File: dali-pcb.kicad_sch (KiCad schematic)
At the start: 6 parts

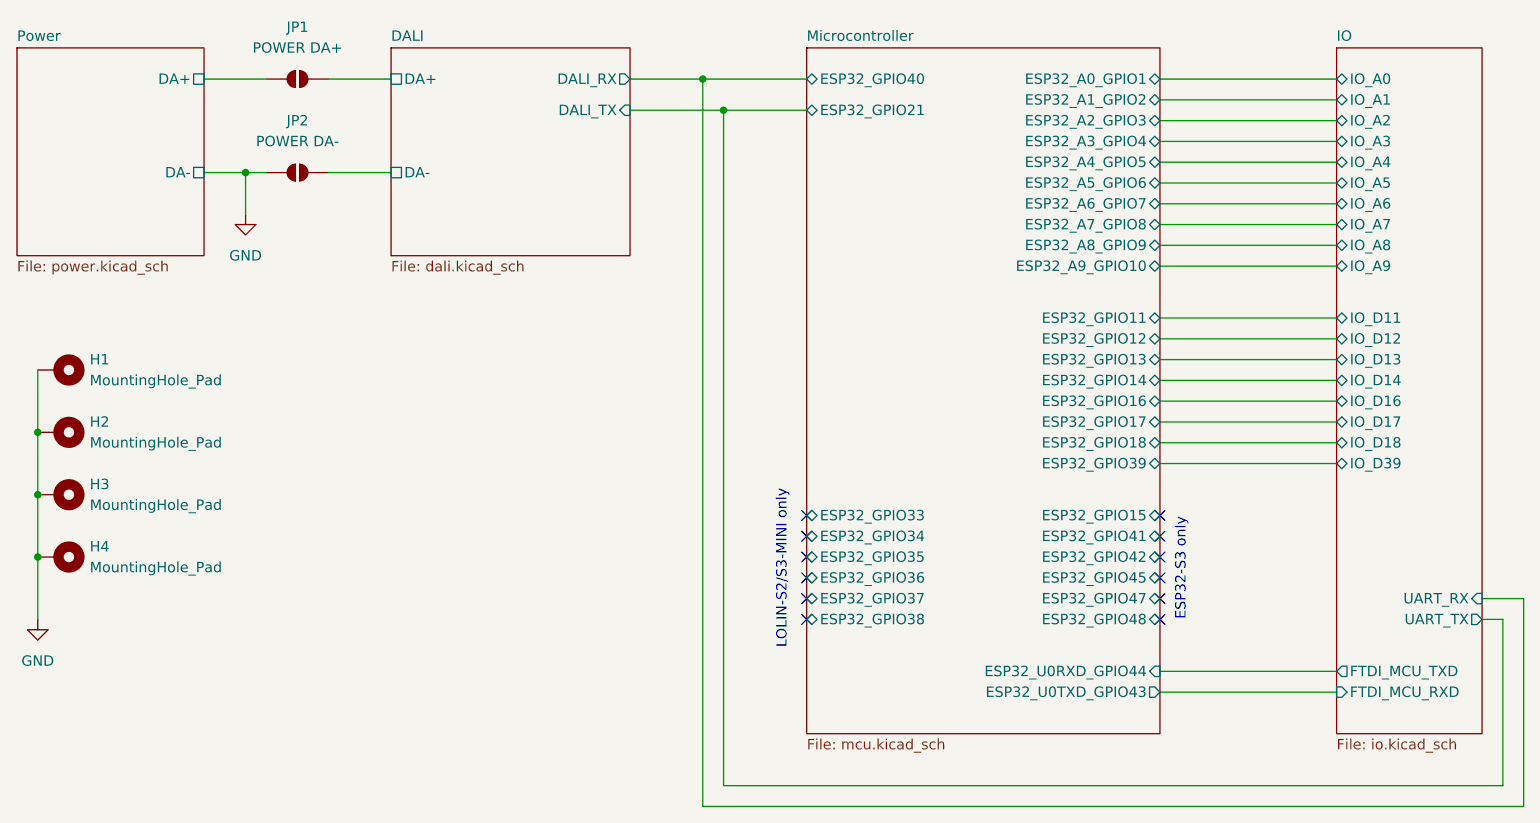
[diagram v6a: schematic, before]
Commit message: Don't connect unused GPIOs together across MCUs
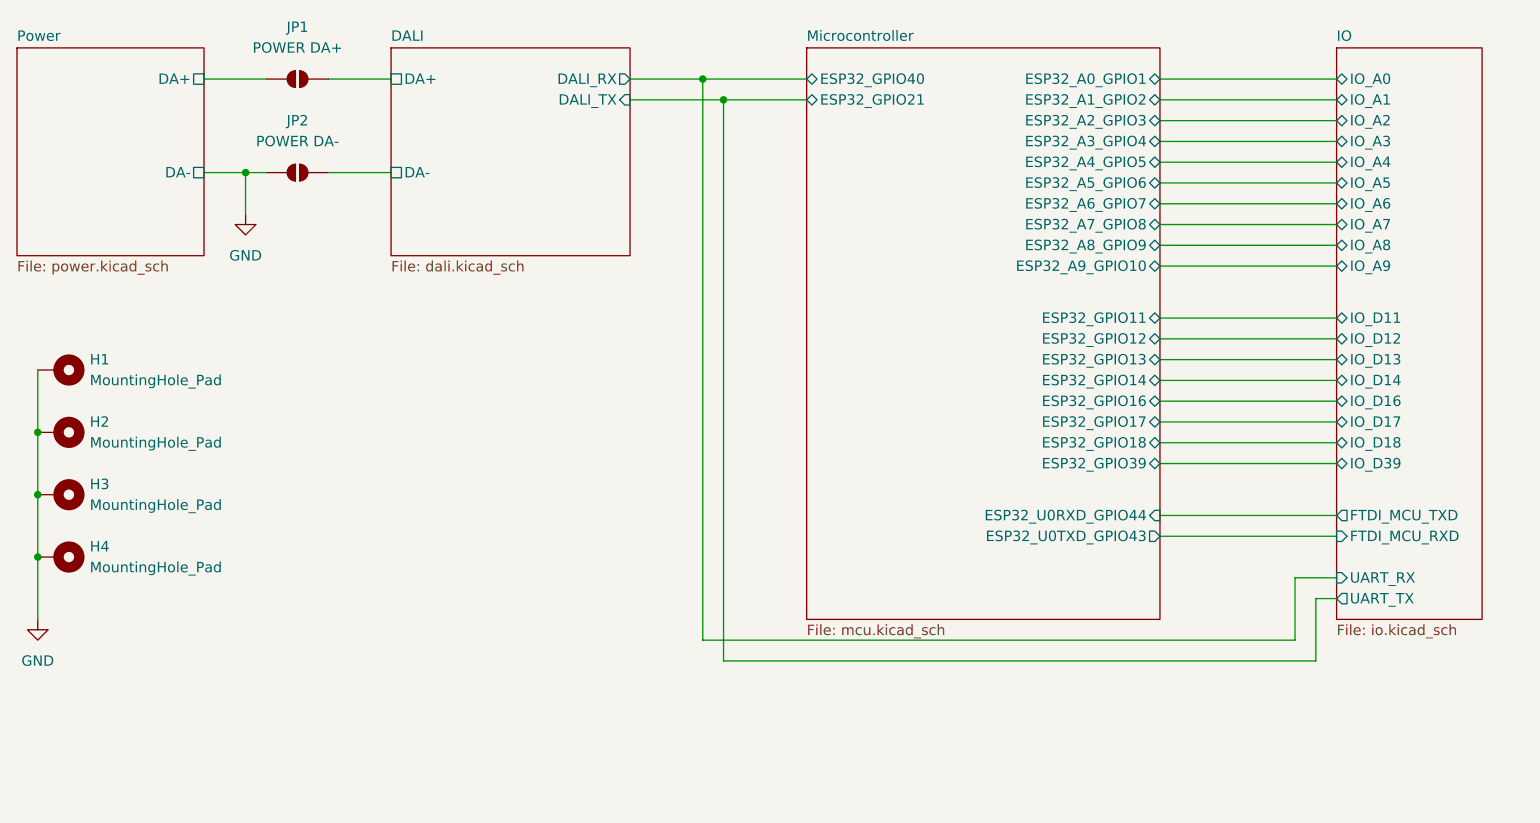
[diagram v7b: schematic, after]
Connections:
- no-connect marks 12 -> 0
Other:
- sheet Microcontroller ports: added none; removed ESP32_GPIO15, ESP32_GPIO33, ESP32_GPIO34, ESP32_GPIO35, ESP32_GPIO36, ESP32_GPIO37, ESP32_GPIO38, ESP32_GPIO41, ESP32_GPIO42, ESP32_GPIO45, ESP32_GPIO47, ESP32_GPIO48
- note removed: "ESP32-S3 only"
- note removed: "LOLIN-S2/S3-MINI only"
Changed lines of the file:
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@@
 	(generator_version "9.0")
 	(paper "User" 195 105)
-	(text "LOLIN-S2/S3-MINI only"
-		(exclude_from_sim no)
-		(at 98.552 70.104 90)
-		(effects
-			(font
-				(size 1.27 1.27)
-			)
-		)
-	)
-	(text "ESP32-S3 only"
-		(exclude_from_sim no)
-		(at 147.32 70.104 90)
-		(effects
-			(font
-				(size 1.27 1.27)
-			)
-		)
-	)
 	(junction
 		(at 7.62 68.58)
@@
 	)
 	(junction
+		(at 91.44 12.7)
+		(diameter 0)
+		(color 0 0 0 0)
+	)
+	(junction
 		(at 7.62 60.96)
 		(diameter 0)
@@
 		(color 0 0 0 0)
 	)
-	(junction
-		(at 91.44 13.97)
-		(diameter 0)
-		(color 0 0 0 0)
-	)
-	(no_connect
-		(at 101.6 66.04)
-	)
-	(no_connect
-		(at 144.78 68.58)
-	)
-	(no_connect
-		(at 101.6 73.66)
-	)
-	(no_connect
-		(at 101.6 71.12)
-	)
-	(no_connect
-		(at 144.78 71.12)
-	)
-	(no_connect
-		(at 101.6 76.2)
-	)
-	(no_connect
-		(at 101.6 68.58)
-	)
-	(no_connect
-		(at 144.78 63.5)
-	)
-	(no_connect
-		(at 144.78 73.66)
-	)
-	(no_connect
-		(at 144.78 76.2)
-	)
-	(no_connect
-		(at 144.78 66.04)
-	)
-	(no_connect
-		(at 101.6 63.5)
-	)
 	(wire
 		(pts
@@
 	(wire
 		(pts
-			(xy 186.69 96.52) (xy 91.44 96.52)
+			(xy 163.83 81.28) (xy 91.44 81.28)
 		)
 		(stroke
@@
 	(wire
 		(pts
-			(xy 189.23 73.66) (xy 189.23 99.06)
+			(xy 161.29 71.12) (xy 161.29 78.74)
 		)
 		(stroke
@@
 	(wire
 		(pts
-			(xy 189.23 99.06) (xy 88.9 99.06)
+			(xy 161.29 78.74) (xy 88.9 78.74)
 		)
 		(stroke
@@
 	(wire
 		(pts
-			(xy 91.44 13.97) (xy 101.6 13.97)
+			(xy 91.44 12.7) (xy 101.6 12.7)
 		)
 		(stroke
@@
 	(wire
 		(pts
-			(xy 80.01 13.97) (xy 91.44 13.97)
-		)
-		(stroke
-			(width 0)
-			(type default)
-		)
-	)
-	(wire
-		(pts
-			(xy 91.44 13.97) (xy 91.44 96.52)
+			(xy 80.01 12.7) (xy 91.44 12.7)
 		)
 		(stroke
@@
 	(wire
 		(pts
-			(xy 144.78 85.09) (xy 166.37 85.09)
+			(xy 144.78 66.04) (xy 166.37 66.04)
 		)
 		(stroke
@@
 	(wire
 		(pts
-			(xy 184.15 76.2) (xy 186.69 76.2)
+			(xy 163.83 73.66) (xy 166.37 73.66)
 		)
 		(stroke
@@
 	(wire
 		(pts
-			(xy 144.78 82.55) (xy 166.37 82.55)
+			(xy 144.78 63.5) (xy 166.37 63.5)
 		)
 		(stroke
@@
 	(wire
 		(pts
-			(xy 88.9 10.16) (xy 88.9 99.06)
+			(xy 88.9 10.16) (xy 88.9 78.74)
+		)
+		(stroke
+			(width 0)
+			(type default)
+		)
+	)
+	(wire
+		(pts
+			(xy 161.29 71.12) (xy 166.37 71.12)
 		)
 		(stroke
@@
 	(wire
 		(pts
-			(xy 186.69 76.2) (xy 186.69 96.52)
+			(xy 163.83 73.66) (xy 163.83 81.28)
 		)
 		(stroke
@@
 	(wire
 		(pts
-			(xy 184.15 73.66) (xy 189.23 73.66)
+			(xy 91.44 12.7) (xy 91.44 81.28)
 		)
 		(stroke
@@
 	(sheet
 		(at 166.37 6.35)
-		(size 17.78 83.82)
+		(size 17.78 69.85)
 		(exclude_from_sim no)
 		(in_bom yes)
@@
 		)
 		(property "Sheetfile" "io.kicad_sch"
-			(at 166.37 90.7546 0)
+			(at 166.37 76.7846 0)
 			(effects
 				(font
@@
 		)
 		(pin "FTDI_MCU_RXD" input
-			(at 166.37 85.09 180)
+			(at 166.37 66.04 180)
 			(effects
 				(font
@@
 		)
 		(pin "FTDI_MCU_TXD" output
-			(at 166.37 82.55 180)
+			(at 166.37 63.5 180)
 			(effects
 				(font
@@
 		)
 		(pin "UART_RX" input
-			(at 184.15 73.66 0)
-			(effects
-				(font
-					(size 1.27 1.27)
-				)
-				(justify right)
+			(at 166.37 71.12 180)
+			(effects
+				(font
+					(size 1.27 1.27)
+				)
+				(justify left)
 			)
 		)
 		(pin "UART_TX" output
-			(at 184.15 76.2 0)
-			(effects
-				(font
-					(size 1.27 1.27)
-				)
-				(justify right)
+			(at 166.37 73.66 180)
+			(effects
+				(font
+					(size 1.27 1.27)
+				)
+				(justify left)
 			)
 		)
@@
 	(sheet
 		(at 101.6 6.35)
-		(size 43.18 83.82)
+		(size 43.18 69.85)
 		(exclude_from_sim no)
 		(in_bom yes)
@@
 		)
 		(property "Sheetfile" "mcu.kicad_sch"
-			(at 101.6 90.7546 0)
+			(at 101.6 76.7846 0)
 			(effects
 				(font
@@
 			)
 		)
-		(pin "ESP32_GPIO15" bidirectional
-			(at 144.78 63.5 0)
-			(effects
-				(font
-					(size 1.27 1.27)
-				)
-				(justify right)
-			)
-		)
 		(pin "ESP32_GPIO16" bidirectional
 			(at 144.78 49.53 0)
@@
 		)
 		(pin "ESP32_GPIO21" bidirectional
-			(at 101.6 13.97 180)
+			(at 101.6 12.7 180)
 			(effects
 				(font
@@
 			)
 		)
-		(pin "ESP32_GPIO41" bidirectional
+		(pin "ESP32_U0RXD_GPIO44" input
+			(at 144.78 63.5 0)
+			(effects
+				(font
+					(size 1.27 1.27)
+				)
+				(justify right)
+			)
+		)
+		(pin "ESP32_U0TXD_GPIO43" output
 			(at 144.78 66.04 0)
 			(effects
@@
 				)
 				(justify right)
-			)
-		)
-		(pin "ESP32_GPIO42" bidirectional
-			(at 144.78 68.58 0)
-			(effects
-				(font
-					(size 1.27 1.27)
-				)
-				(justify right)
-			)
-		)
-		(pin "ESP32_GPIO45" bidirectional
-			(at 144.78 71.12 0)
-			(effects
-				(font
-					(size 1.27 1.27)
-				)
-				(justify right)
-			)
-		)
-		(pin "ESP32_GPIO47" bidirectional
-			(at 144.78 73.66 0)
-			(effects
-				(font
-					(size 1.27 1.27)
-				)
-				(justify right)
-			)
-		)
-		(pin "ESP32_GPIO48" bidirectional
-			(at 144.78 76.2 0)
-			(effects
-				(font
-					(size 1.27 1.27)
-				)
-				(justify right)
-			)
-		)
-		(pin "ESP32_U0RXD_GPIO44" input
-			(at 144.78 82.55 0)
-			(effects
-				(font
-					(size 1.27 1.27)
-				)
-				(justify right)
-			)
-		)
-		(pin "ESP32_U0TXD_GPIO43" output
-			(at 144.78 85.09 0)
-			(effects
-				(font
-					(size 1.27 1.27)
-				)
-				(justify right)
-			)
-		)
-		(pin "ESP32_GPIO33" bidirectional
-			(at 101.6 63.5 180)
-			(effects
-				(font
-					(size 1.27 1.27)
-				)
-				(justify left)
-			)
-		)
-		(pin "ESP32_GPIO34" bidirectional
-			(at 101.6 66.04 180)
-			(effects
-				(font
-					(size 1.27 1.27)
-				)
-				(justify left)
-			)
-		)
-		(pin "ESP32_GPIO35" bidirectional
-			(at 101.6 68.58 180)
-			(effects
-				(font
-					(size 1.27 1.27)
-				)
-				(justify left)
-			)
-		)
-		(pin "ESP32_GPIO36" bidirectional
-			(at 101.6 71.12 180)
-			(effects
-				(font
-					(size 1.27 1.27)
-				)
-				(justify left)
-			)
-		)
-		(pin "ESP32_GPIO37" bidirectional
-			(at 101.6 73.66 180)
-			(effects
-				(font
-					(size 1.27 1.27)
-				)
-				(justify left)
-			)
-		)
-		(pin "ESP32_GPIO38" bidirectional
-			(at 101.6 76.2 180)
-			(effects
-				(font
-					(size 1.27 1.27)
-				)
-				(justify left)
 			)
 		)
@@
 		)
 		(pin "DALI_TX" input
-			(at 80.01 13.97 0)
-			(effects
-				(font
+			(at 80.01 12.7 0)
+			(effects
+				(font

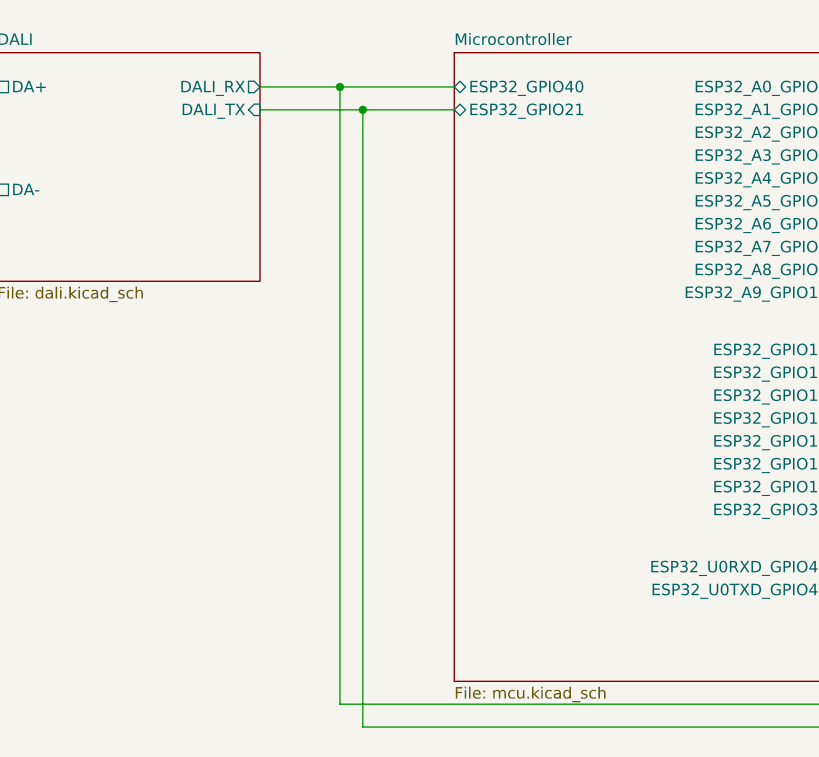
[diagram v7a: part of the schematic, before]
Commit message: First routing attempt
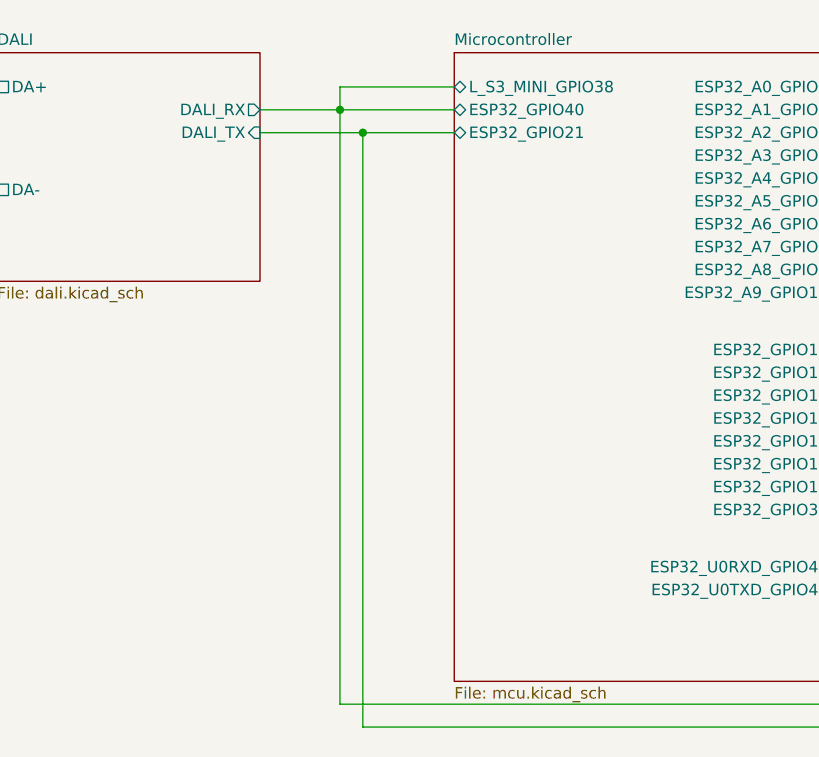
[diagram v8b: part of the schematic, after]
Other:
- sheet Microcontroller ports: added L_S3_MINI_GPIO38; removed none
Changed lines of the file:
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@@
+	)
+	(junction
+		(at 88.9 12.7)
+		(diameter 0)
+		(color 0 0 0 0)
 	)
 	(junction
@@
 	)
 	(junction
-		(at 91.44 12.7)
-		(diameter 0)
-		(color 0 0 0 0)
-	)
-	(junction
 		(at 7.62 60.96)
 		(diameter 0)
@@
 	)
 	(junction
-		(at 88.9 10.16)
+		(at 91.44 15.24)
 		(diameter 0)
 		(color 0 0 0 0)
@@
 	(wire
 		(pts
+			(xy 88.9 10.16) (xy 88.9 12.7)
+		)
+		(stroke
+			(width 0)
+			(type default)
+		)
+	)
+	(wire
+		(pts
 			(xy 7.62 53.34) (xy 7.62 60.96)
 		)
@@
 	(wire
 		(pts
-			(xy 91.44 12.7) (xy 101.6 12.7)
+			(xy 91.44 15.24) (xy 101.6 15.24)
+		)
+		(stroke
+			(width 0)
+			(type default)
+		)
+	)
+	(wire
+		(pts
+			(xy 88.9 12.7) (xy 88.9 78.74)
 		)
 		(stroke
@@
 	(wire
 		(pts
-			(xy 80.01 12.7) (xy 91.44 12.7)
+			(xy 80.01 15.24) (xy 91.44 15.24)
 		)
 		(stroke
@@
 	(wire
 		(pts
+			(xy 91.44 15.24) (xy 91.44 81.28)
+		)
+		(stroke
+			(width 0)
+			(type default)
+		)
+	)
+	(wire
+		(pts
 			(xy 144.78 66.04) (xy 166.37 66.04)
 		)
@@
 	(wire
 		(pts
-			(xy 80.01 10.16) (xy 88.9 10.16)
+			(xy 80.01 12.7) (xy 88.9 12.7)
 		)
 		(stroke
@@
 	(wire
 		(pts
-			(xy 88.9 10.16) (xy 101.6 10.16)
+			(xy 88.9 12.7) (xy 101.6 12.7)
 		)
 		(stroke
@@
 	(wire
 		(pts
-			(xy 88.9 10.16) (xy 88.9 78.74)
+			(xy 101.6 10.16) (xy 88.9 10.16)
 		)
 		(stroke
@@
 		(pts
 			(xy 33.02 21.59) (xy 35.56 21.59)
-		)
-		(stroke
-			(width 0)
-			(type default)
-		)
-	)
-	(wire
-		(pts
-			(xy 91.44 12.7) (xy 91.44 81.28)
 		)
 		(stroke
@@
 		)
 		(pin "ESP32_GPIO21" bidirectional
-			(at 101.6 12.7 180)
+			(at 101.6 15.24 180)
 			(effects
 				(font
@@
 		)
 		(pin "ESP32_GPIO40" bidirectional
-			(at 101.6 10.16 180)
+			(at 101.6 12.7 180)
 			(effects
 				(font
@@
 				)
 				(justify right)
+			)
+		)
+		(pin "L_S3_MINI_GPIO38" bidirectional
+			(at 101.6 10.16 180)
+			(effects
+				(font
+					(size 1.27 1.27)
+				)
+				(justify left)
 			)
 		)
@@
 		)
 		(pin "DALI_RX" output
-			(at 80.01 10.16 0)
+			(at 80.01 12.7 0)
 			(effects
 				(font
@@
 		)
 		(pin "DALI_TX" input
-			(at 80.01 12.7 0)
-			(effects
-				(font
+			(at 80.01 15.24 0)
+			(effects
+				(font
